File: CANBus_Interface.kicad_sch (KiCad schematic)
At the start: 33 parts, among them CN2 SM04B-SURS-TF(LF)(SN), U4 TCAN4550RGYRQ1, Y1 40MHz

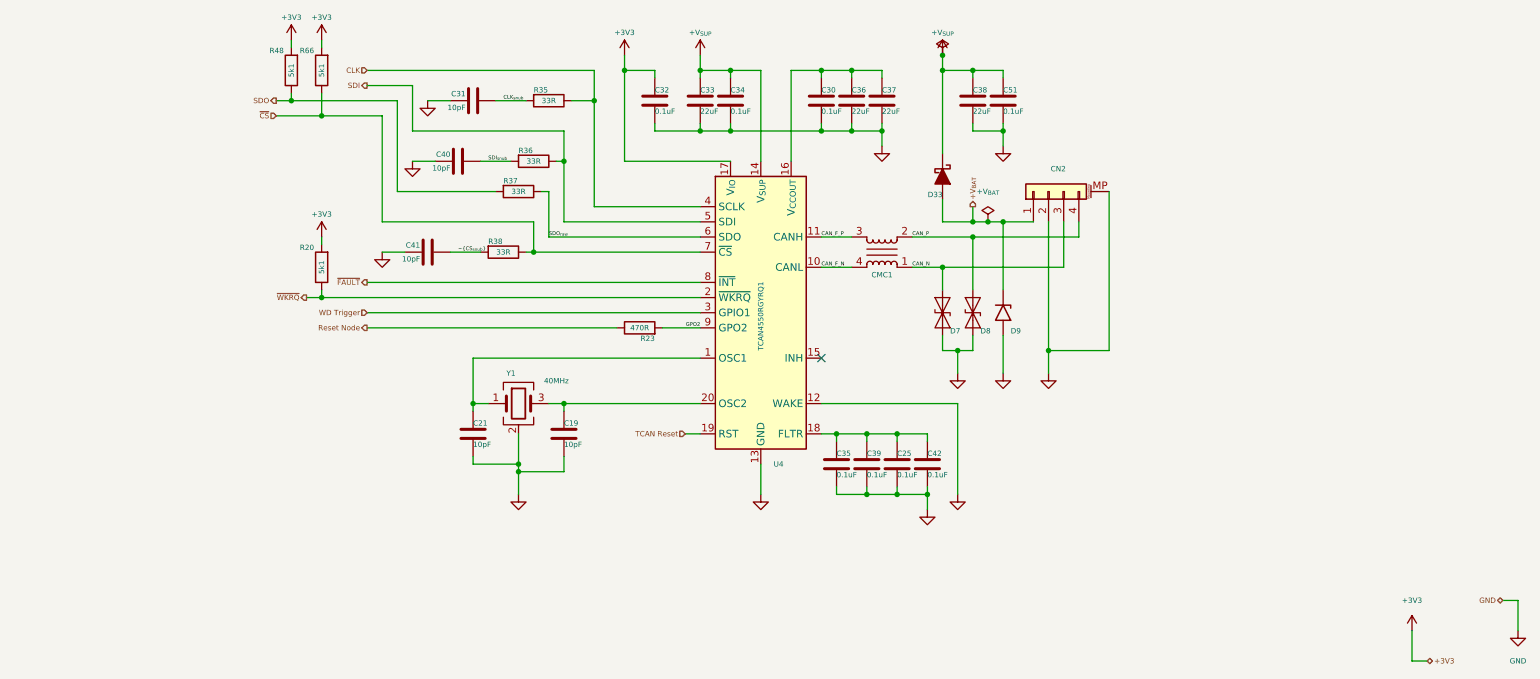
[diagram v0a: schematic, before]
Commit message: Update CANBus_Interface.kicad_sch, ESP32-S3 D1 Pico Board.kicad_sch, ESP32-S3 Pico D1.kicad_pcb, and 15 more files
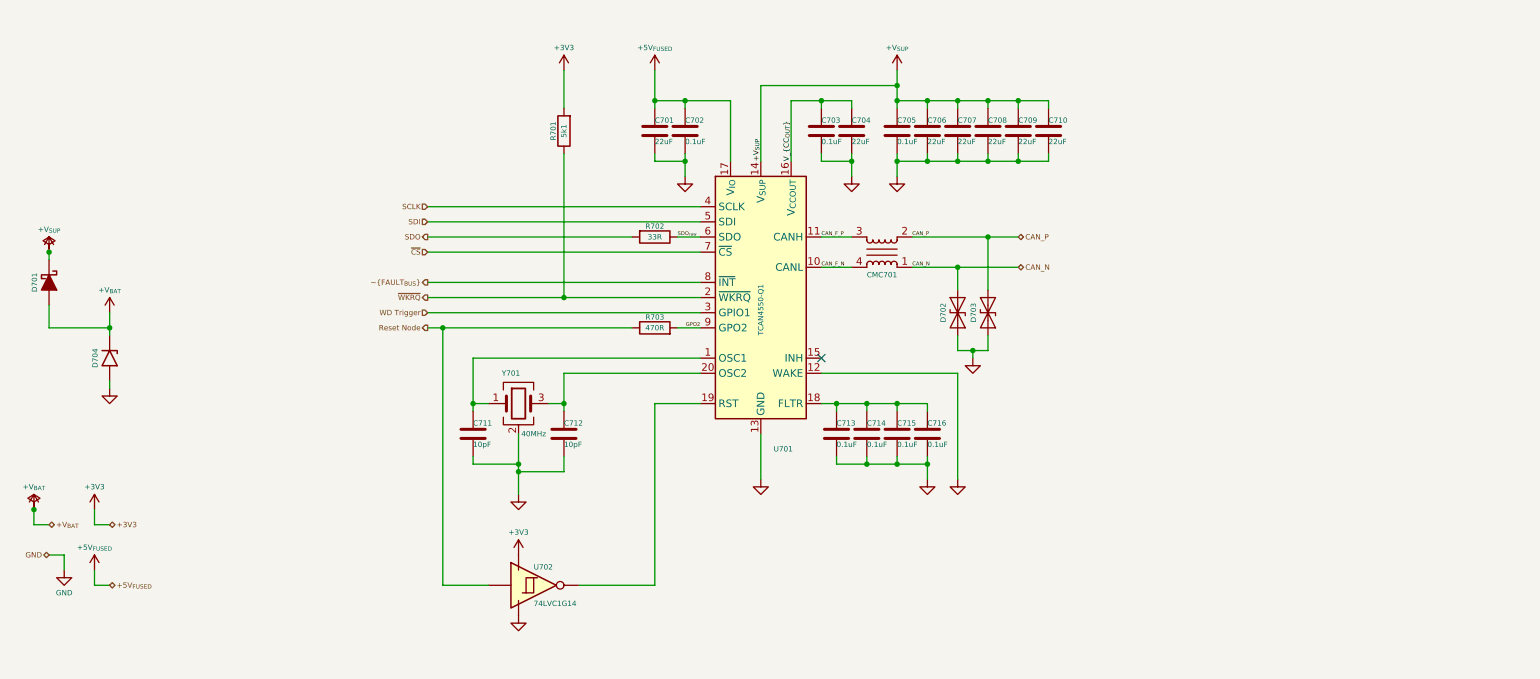
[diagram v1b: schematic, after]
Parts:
- removed C31, C40, C41: 10pF, Capacitors:C_0201_Dense, symbol Device:C
- removed C38: 22uF, Capacitors:C_0603_Dense, symbol Device:C
- removed C51: 0.1uF, Capacitors:C_0201_Dense, symbol Device:C
- removed CN2: SM04B-SURS-TF(LF)(SN), Personal_FootprintLibrary:JST_SUH_1x04_MP_P0.8mm, symbol PersonalSchematicSymbolLibrary:Conn_01x04_MountingPin
- removed R35, R36, R38: 33R, Resistors:R_0201_Dense, symbol Device:R
- removed R48, R66: 5k1, Resistors:R_0201_Dense, symbol Device:R
- added C707, C708, C709, C710: 22uF, My Capacitors:C_0603_Dense, symbol Device:C
- added U702: 74LVC1G14, Personal_FootprintLibrary:X2SON5_SOT1226_0.8x0.8mm, symbol 74xxx1Gyy:74LVC1G14
- C701: renamed from C37; footprint Capacitors:C_0603_Dense -> My Capacitors:C_0603_Dense; Distributor Link 1 https://www.digikey.com/en/products/detail/samsung-electro-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 -> https://www.digikey.com/en/products/detail/murata-electroni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; Distributor Link 2 https://www.mouser.com/ProductDetail/Samsung-Electro-Mechan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 -> https://www.mouser.com/ProductDetail/Murata-Electronics/GRM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; LCSC C2762594 -> C29519229; Manufacturer Samsung Electro-Mechanics -> Murata Electronics; Manufacturer Part Number CL10A226MO7JZNC -> GRM188C61E226ME01D
- C702: renamed from C32; footprint Capacitors:C_0201_Dense -> My Capacitors:C_0201_Dense
- C703: renamed from C30; footprint Capacitors:C_0201_Dense -> My Capacitors:C_0201_Dense
- C704: renamed from C36; footprint Capacitors:C_0603_Dense -> My Capacitors:C_0603_Dense; Distributor Link 1 https://www.digikey.com/en/products/detail/samsung-electro-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 -> https://www.digikey.com/en/products/detail/murata-electroni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; Distributor Link 2 https://www.mouser.com/ProductDetail/Samsung-Electro-Mechan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 -> https://www.mouser.com/ProductDetail/Murata-Electronics/GRM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; LCSC C2762594 -> C29519229; Manufacturer Samsung Electro-Mechanics -> Murata Electronics; Manufacturer Part Number CL10A226MO7JZNC -> GRM188C61E226ME01D
- C705: renamed from C34; footprint Capacitors:C_0201_Dense -> My Capacitors:C_0201_Dense
- C706: renamed from C33; footprint Capacitors:C_0603_Dense -> My Capacitors:C_0603_Dense; Distributor Link 1 https://www.digikey.com/en/products/detail/samsung-electro-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 -> https://www.digikey.com/en/products/detail/murata-electroni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; Distributor Link 2 https://www.mouser.com/ProductDetail/Samsung-Electro-Mechan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 -> https://www.mouser.com/ProductDetail/Murata-Electronics/GRM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; LCSC C2762594 -> C29519229; Manufacturer Samsung Electro-Mechanics -> Murata Electronics; Manufacturer Part Number CL10A226MO7JZNC -> GRM188C61E226ME01D
- C711: renamed from C21; footprint Capacitors:C_0201_Dense -> My Capacitors:C_0201_Dense
- C712: renamed from C19; footprint Capacitors:C_0201_Dense -> My Capacitors:C_0201_Dense
- C713: renamed from C35; footprint Capacitors:C_0201_Dense -> My Capacitors:C_0201_Dense
- C714: renamed from C39; footprint Capacitors:C_0201_Dense -> My Capacitors:C_0201_Dense
- C715: renamed from C25; footprint Capacitors:C_0201_Dense -> My Capacitors:C_0201_Dense
- C716: renamed from C42; footprint Capacitors:C_0201_Dense -> My Capacitors:C_0201_Dense
- D701: renamed from D33; value SDM1100LP-7 -> PMEG4002ESFYL; footprint Personal_FootprintLibrary:DFN2020-2 -> Personal_FootprintLibrary:DSN0603-2; Distributor Link 1 https://www.digikey.com/en/products/detail/diodes-incorpora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 -> https://www.digikey.com/en/products/detail/nexperia-usa-inc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; Distributor Link 2 https://www.mouser.com/ProductDetail/Diodes-Incorporated/SD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 -> https://www.mouser.com/ProductDetail/Nexperia/PMEG4002ESFYL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; LCSC C6999905 -> C22435168; Manufacturer Diodes Incorporated -> Nexperia USA Inc.; Manufacturer Part Number SDM1100LP-7 -> PMEG4002ESFYL
- R701: renamed from R20; footprint Resistors:R_0201_Dense -> My Resistors:R_0201_Dense
- R702: renamed from R37; footprint Resistors:R_0201_Dense -> My Resistors:R_0201_Dense
- R703: renamed from R23; footprint Resistors:R_0201_Dense -> My Resistors:R_0201_Dense
- U701: renamed from U4; value TCAN4550RGYRQ1 -> TCAN4550-Q1
- renumbered CMC1 to CMC701, D7 to D702, D8 to D703, D9 to D704, Y1 to Y701
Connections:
- net +3V3: now also U702.EP (VCC); no longer C702.1, U701.17 (V_{IO})
- net +V_{SUP}: now also C707.1, C708.1, C709.1, C710.1
- net GND: now also C707.2, C708.2, C709.2, C710.2, U702.3 (GND)
- net Reset Node: now also U702.2 (A)
- net V_{CC_{OUT}}: now reaches C703.1, C704.1, U701.16 (V_{CCOUT})
- net V_{CC_{OUT}}: no longer C701.1
- net CLK renamed SCLK
- net TCAN Reset: no longer names the net of U701.19 (RST)
- net TCAN Reset: now also U702.4 (Y)
- net ~{FAULT} renamed ~{FAULT_{BUS}}
- new net +5V_{FUSED}: C701.1, C702.1, U701.17 (V_{IO})
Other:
- moved on the sheet: C701, C702, C703, C704, C705, C706, C713, C714, C715, C716, D701, D702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
